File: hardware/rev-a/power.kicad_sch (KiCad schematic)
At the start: 27 parts, among them J1 USB_C_Receptacle_PowerOnly_6P, J2 Conn_01x02, U1 TLV75533PDBV, U2 BQ24074RGT

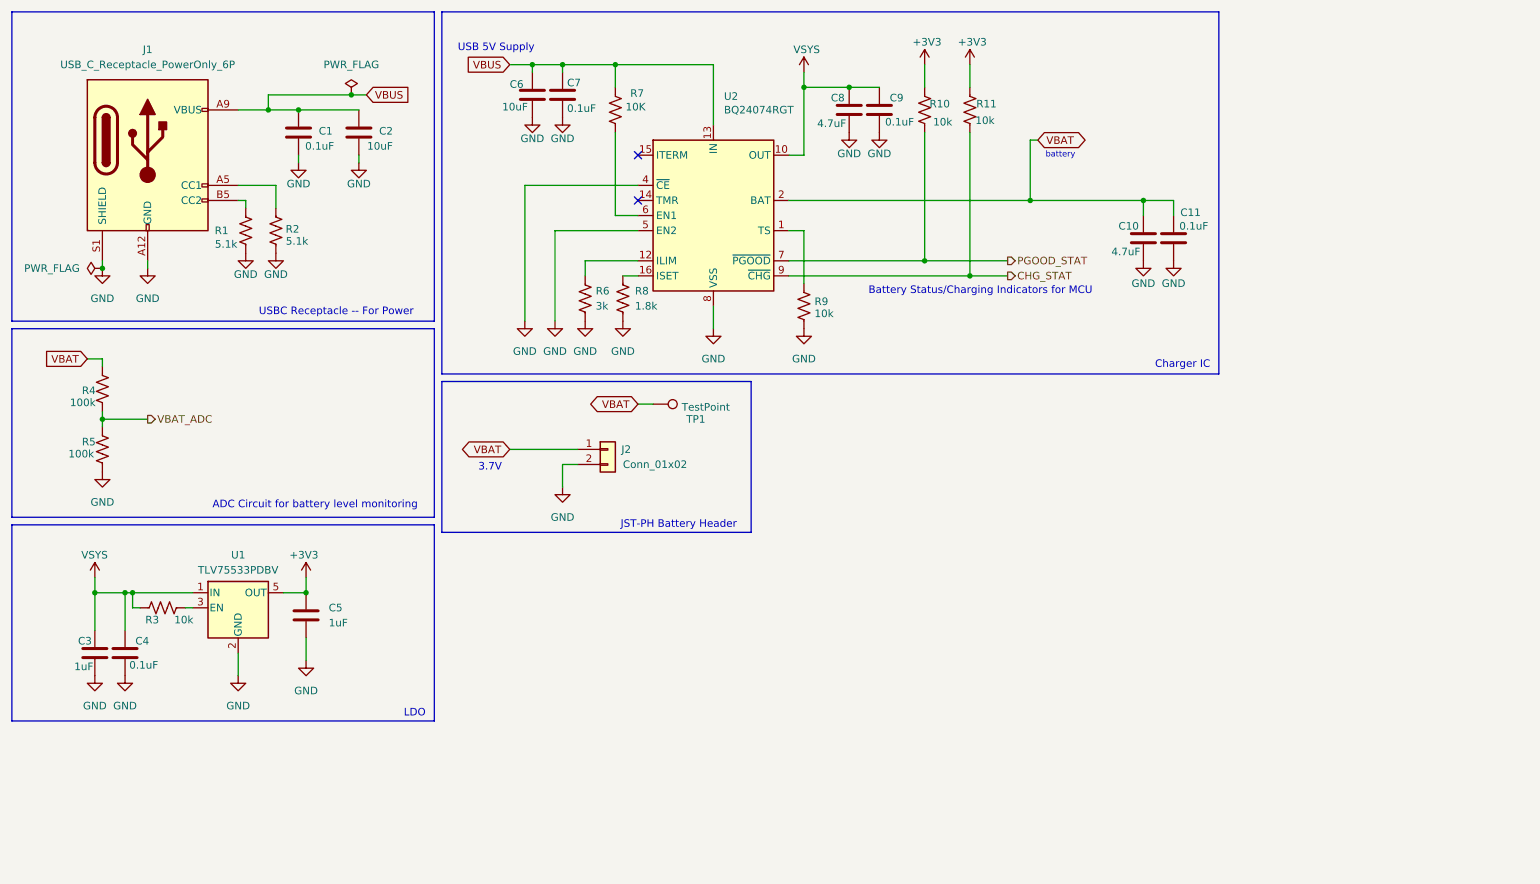
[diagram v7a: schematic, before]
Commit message: rev c with labeled ICs
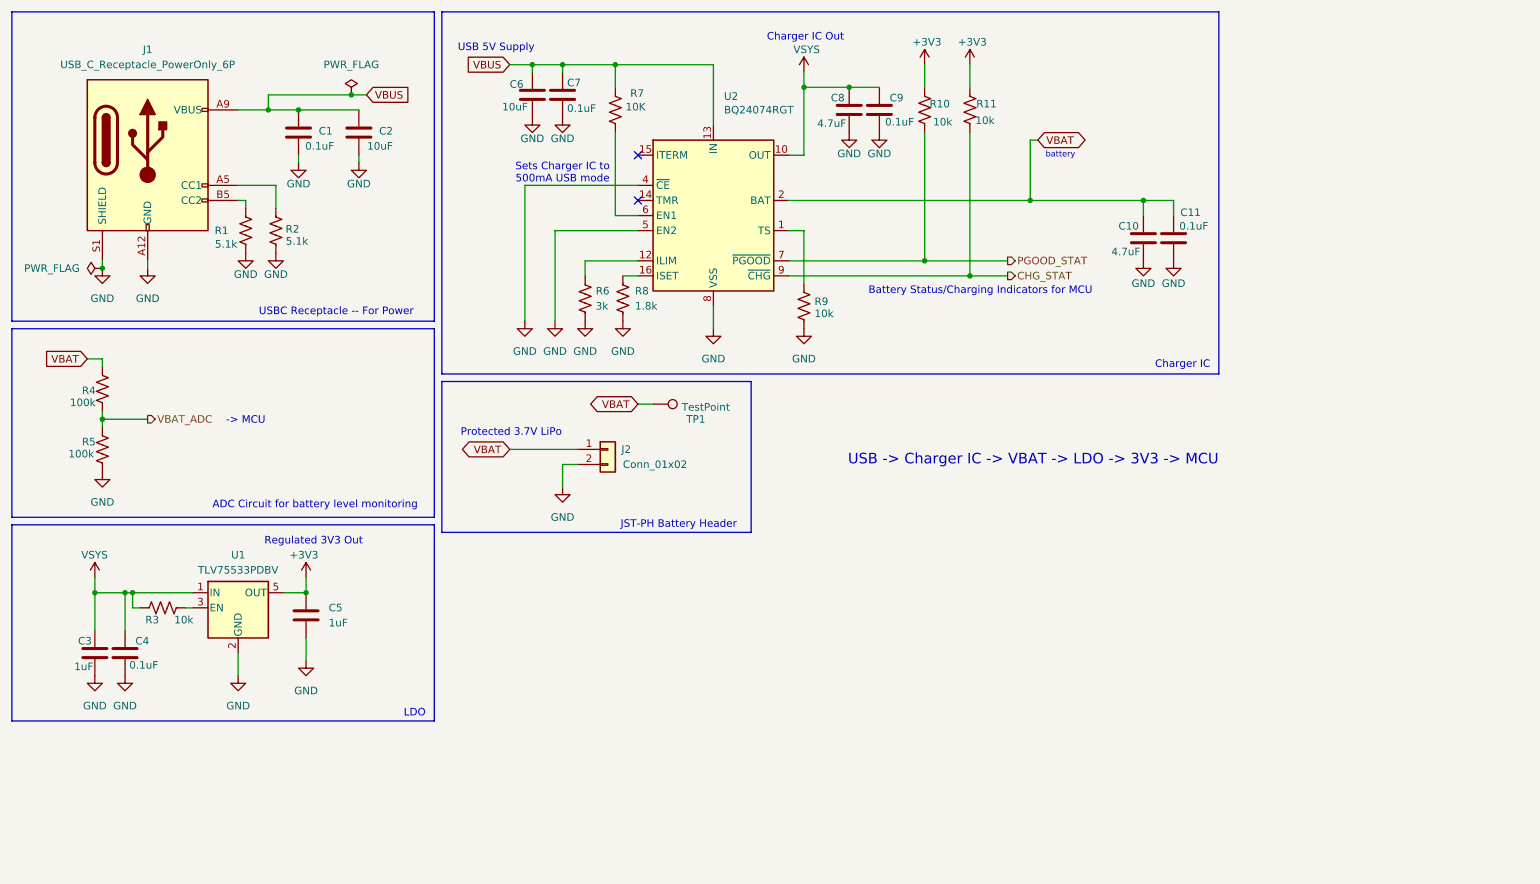
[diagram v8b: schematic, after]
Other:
- note added: "-> MCU"
- note added: "Charger IC Out"
- note added: "Protected 3.7V LiPo"
- note added: "Regulated 3V3 Out"
- note added: "Sets Charger IC to 500mA USB mode"
- note added: "USB -> Charger IC -> VBAT -> LDO -> 3V3 -> MCU"
- note removed: "3.7V"
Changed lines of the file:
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@@
 	(generator "eeschema")
 	(generator_version "9.0")
-	(paper "A4")
+	(paper "User" 254 152.4)
 	(title_block
 		(title "power sheet")
@@
 		)
 	)
-	(text "3.7V"
+	(text "Protected 3.7V LiPo"
 		(exclude_from_sim no)
-		(at 93.218 89.408 0)
+		(at 96.774 83.566 0)
 		(effects
 			(font
@@
 		)
 	)
+	(text "Regulated 3V3 Out"
+		(exclude_from_sim no)
+		(at 63.5 101.854 0)
+		(effects
+			(font
+				(size 1.27 1.27)
+			)
+		)
+	)
+	(text "USB -> Charger IC -> VBAT -> LDO -> 3V3 -> MCU"
+		(exclude_from_sim no)
+		(at 184.658 88.138 0)
+		(effects
+			(font
+				(size 1.778 1.778)
+			)
+		)
+	)
+	(text "-> MCU"
+		(exclude_from_sim no)
+		(at 52.07 81.534 0)
+		(effects
+			(font
+				(size 1.27 1.27)
+			)
+		)
+	)
+	(text "Sets Charger IC to\n500mA USB mode"
+		(exclude_from_sim no)
+		(at 105.41 39.878 0)
+		(effects
+			(font
+				(size 1.27 1.27)
+			)
+		)
+	)
 	(text "Charger IC"
 		(exclude_from_sim no)
@@
 		(effects
 			(font
+				(size 1.27 1.27)
+			)
+		)
+	)
+	(text "Charger IC Out"
+		(exclude_from_sim no)
+		(at 146.304 17.018 0)
+		(effects
+			(font
